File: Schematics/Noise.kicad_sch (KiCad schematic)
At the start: 116 parts, among them J44 Conn_01x03, J45 Conn_01x03, J46 Conn_01x03, J47 Conn_01x02, J48 Conn_01x02, J49 Conn_01x02, J50 Conn_01x02, Q10 BSS138, Q11 BSS138, Q9 2N3904, U55 TL072, U56 TL074, U57 LM1117-5, U58 LM1117-3.3, U59 PCF8575, U60 TL074, U61 TL074, U62 DG212C, U63 DG212C, U64 TL074, U65 DG212C, U66 DG212C, U67 TL074, U68 TL074

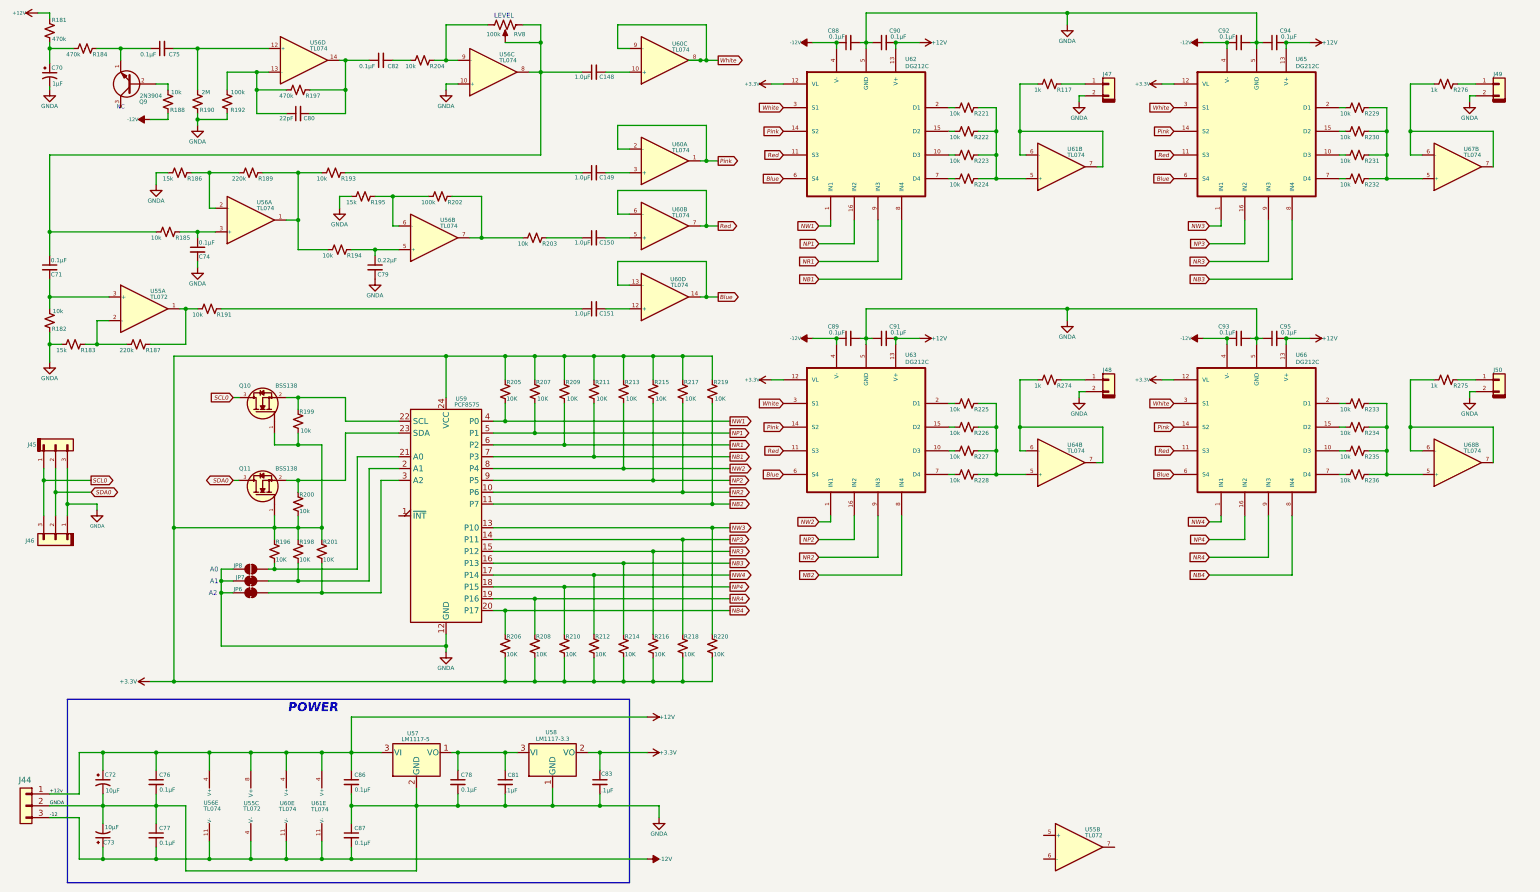
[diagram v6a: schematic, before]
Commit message: All Oscillators have thier own D/A converters and both LFOs are working.  Callibration functions.
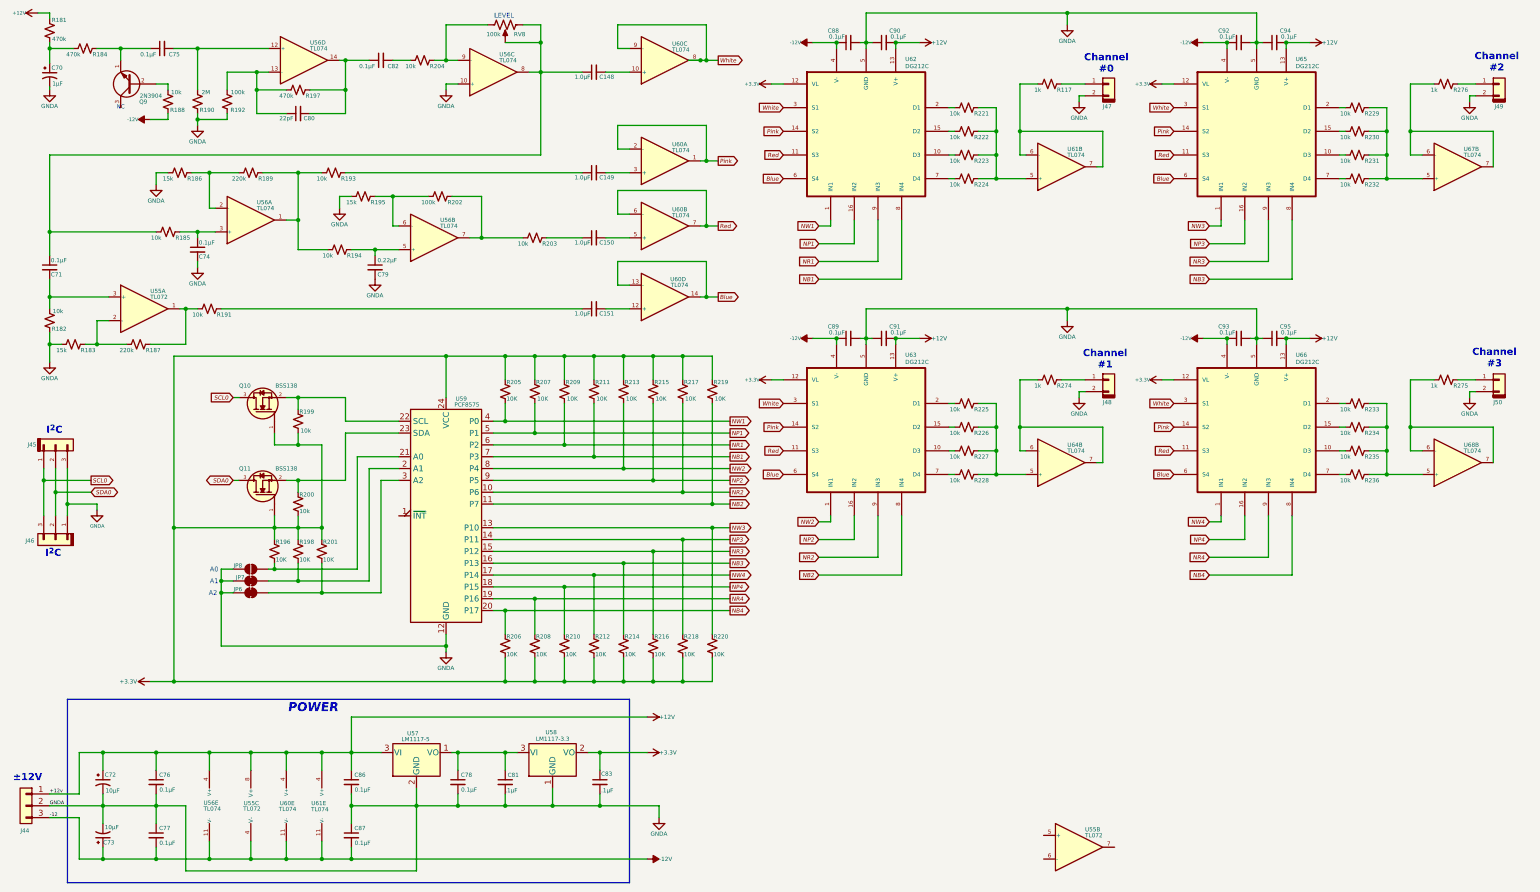
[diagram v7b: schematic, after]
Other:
- note added: "Channel #0"
- note added: "Channel #1"
- note added: "Channel #2"
- note added: "Channel #3"
- note added: "I^{2}C"
- note added: "±12V"
- title: Dual Noise Geneartor -> Quad Noise Geneartor
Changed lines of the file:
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@@
 	(paper "USLegal")
 	(title_block
-		(title "Dual Noise Geneartor")
+		(title "Quad Noise Geneartor")
 		(date "2025-01-16")
 		(rev "4.2")
 		(comment 1 "In Development ")
 	)
+	(text "Channel\n#0"
+		(exclude_from_sim no)
+		(at 249.682 26.162 0)
+		(effects
+			(font
+				(size 1.524 1.524)
+				(thickness 0.3048)
+				(bold yes)
+			)
+		)
+	)
+	(text "Channel\n#2"
+		(exclude_from_sim no)
+		(at 333.502 25.908 0)
+		(effects
+			(font
+				(size 1.524 1.524)
+				(thickness 0.3048)
+				(bold yes)
+			)
+		)
+	)
 	(text "NC"
 		(exclude_from_sim no)
@@
 		)
 	)
+	(text "I^{2}C"
+		(exclude_from_sim no)
+		(at 23.876 104.902 0)
+		(effects
+			(font
+				(size 1.524 1.524)
+				(thickness 0.3048)
+				(bold yes)
+			)
+		)
+	)
 	(text "A2"
 		(exclude_from_sim no)
@@
 		)
 	)
+	(text "I^{2}C"
+		(exclude_from_sim no)
+		(at 23.622 131.318 0)
+		(effects
+			(font
+				(size 1.524 1.524)
+				(thickness 0.3048)
+				(bold yes)
+			)
+		)
+	)
+	(text "Channel\n#3"
+		(exclude_from_sim no)
+		(at 332.994 89.408 0)
+		(effects
+			(font
+				(size 1.524 1.524)
+				(thickness 0.3048)
+				(bold yes)
+			)
+		)
+	)
+	(text "±12V"
+		(exclude_from_sim no)
+		(at 14.986 180.34 0)
+		(effects
+			(font
+				(size 1.524 1.524)
+				(thickness 0.3048)
+				(bold yes)
+			)
+			(justify left bottom)
+		)
+	)
 	(text "A1"
 		(exclude_from_sim no)
@@
 		)
 	)
+	(text "Channel\n#1"
+		(exclude_from_sim no)
+		(at 249.428 89.662 0)
+		(effects
+			(font
+				(size 1.524 1.524)
+				(thickness 0.3048)
+				(bold yes)
+			)
+		)
+	)
 	(text "A0"
 		(exclude_from_sim no)
@@
 		(dnp no)
 		(property "Reference" "J48"
-			(at 248.935 91.8652 0)
+			(at 248.92 98.806 0)
 			(effects
 				(font
@@
 		(dnp no)
 		(property "Reference" "J44"
-			(at 17.5768 179.8828 0)
+			(at 17.526 190.754 0)
 			(effects
 				(font
-					(size 1.27 1.27)
+					(size 0.889 0.889)
 				)
 			)
@@
 		(dnp no)
 		(property "Reference" "J49"
-			(at 332.755 28.3652 0)
+			(at 332.994 35.306 0)
 			(effects
 				(font
@@
 		(dnp no)
 		(property "Reference" "J47"
-			(at 248.935 28.3652 0)
+			(at 248.92 35.306 0)
 			(effects
 				(font
@@
 		(dnp no)
 		(property "Reference" "J50"
-			(at 332.755 91.8652 0)
+			(at 332.74 98.806 0)
 			(effects
 				(font

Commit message: Fixed bugs in voice selection on configuration.  Reorganized schematics to have different master drawings for power and audio paths.  Started work on dual 3-pole state variable filter with resonance.
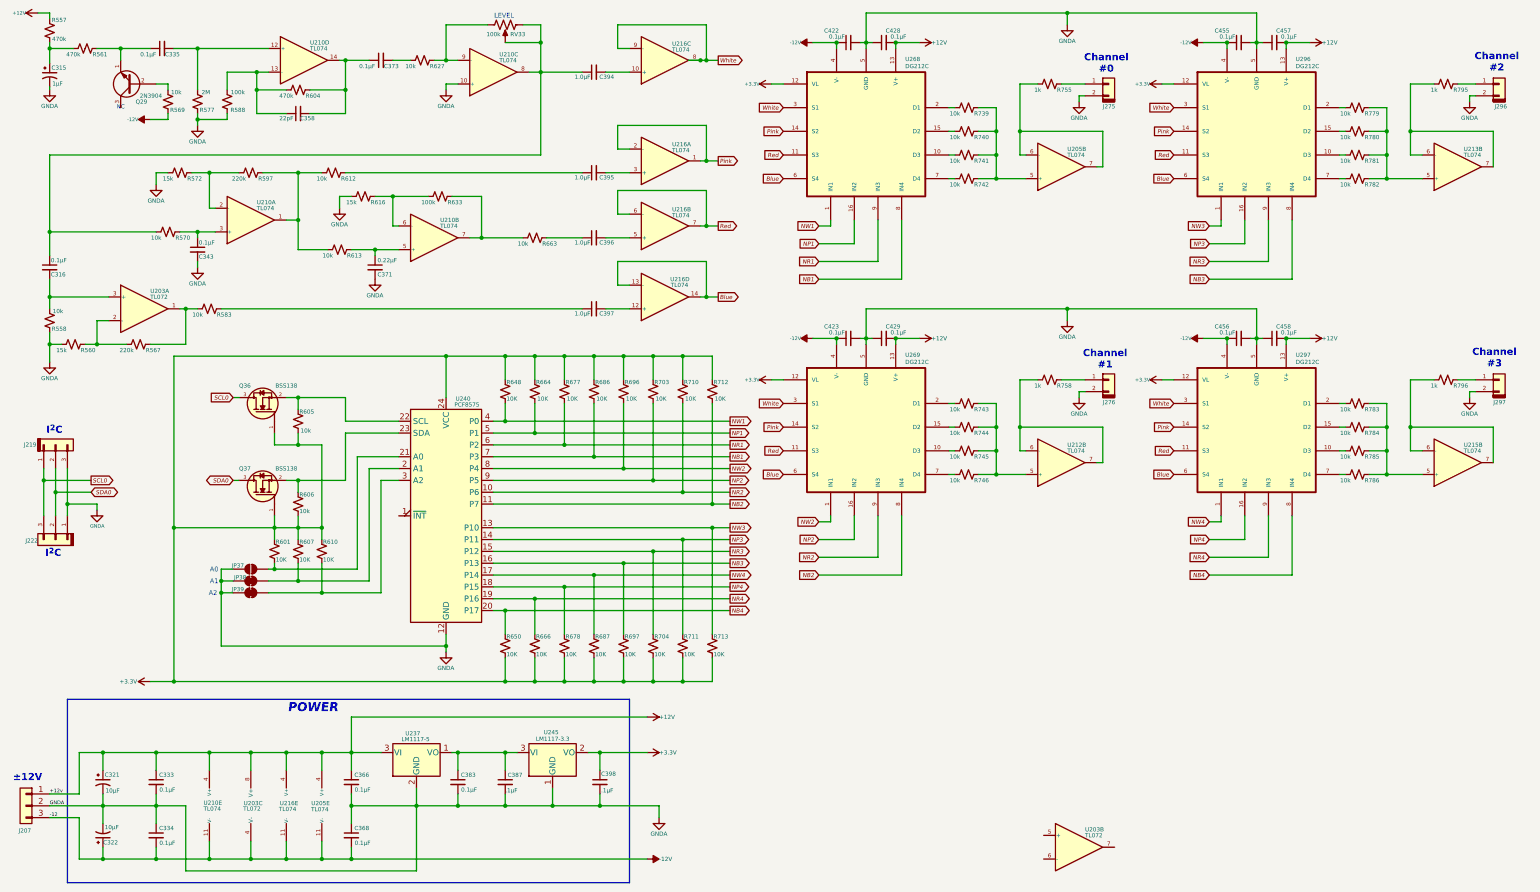
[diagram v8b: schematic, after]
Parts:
- renumbered C70 to C315, C71 to C316, C72 to C321, C73 to C322, C76 to C333, C77 to C334, C75 to C335, C74 to C343, C80 to C358, C86 to C366, C87 to C368, C79 to C371, C82 to C373, C78 to C383, C81 to C387, C148 to C394, C149 to C395, C150 to C396, C151 to C397, C83 to C398, C88 to C422, C89 to C423, C90 to C428, C91 to C429, C92 to C455, C93 to C456, C94 to C457, C95 to C458, J44 to J207, J45 to J219, J46 to J222, J47 to J275, J48 to J276, J49 to J296, J50 to J297, JP8 to JP37, JP7 to JP38, JP6 to JP39, Q9 to Q29, Q10 to Q36, Q11 to Q37, R181 to R557, R182 to R558, R183 to R560, R184 to R561, R187 to R567, R188 to R569, R185 to R570, R186 to R572, R190 to R577, R191 to R583, R192 to R588, R189 to R597, R196 to R601, R197 to R604, R199 to R605, R200 to R606, R198 to R607, R201 to R610, R193 to R612, R194 to R613, R195 to R616, R204 to R627, R202 to R633, R205 to R648, R206 to R650, R203 to R663, R207 to R664, R208 to R666, R209 to R677, R210 to R678, R211 to R686, R212 to R687, R213 to R696, R214 to R697, R215 to R703, R216 to R704, R217 to R710, R218 to R711, R219 to R712, R220 to R713, R221 to R739, R222 to R740, R223 to R741, R224 to R742, R225 to R743, R226 to R744, R227 to R745, R228 to R746, R117 to R755, R274 to R758, R229 to R779, R230 to R780, R231 to R781, R232 to R782, R233 to R783, R234 to R784, R235 to R785, R236 to R786, R276 to R795, R275 to R796, RV8 to RV33, U55 to U203, U61 to U205, U56 to U210, U64 to U212, U67 to U213, U68 to U215, U60 to U216, U57 to U237, U59 to U240, U58 to U245, U62 to U268, U63 to U269, U65 to U296, U66 to U297
